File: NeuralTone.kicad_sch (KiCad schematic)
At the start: 95 parts, among them J1 USB-C PD, J2 Guitar, J3 Headphones, J4 USB-A Port, J5 Line Out, J6 5V Fan, J7 TF-01A, Q1 AON7421, Q2 IRLML6344, SW1 SW_Push, U1 AP2210N-3.3, U2 AP2210N-5.0, U3 CH224K, U4 MCP6022, U5 AMS1084CM-5.0, U6 AP2210N-3.3, U7 AP2171, U8 NAU8814YG, U9 DRTR5V0U2SR, Y1 OT322512MJBA4SL

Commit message: fix all footprints and 3d models
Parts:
- D1, D8: footprint Diode_SMD:D_SOD-123 -> NeuralTone:D_SOD-123
- D10, D6: footprint Package_TO_SOT_SMD:SOT-23-6_Handsoldering -> Package_TO_SOT_SMD:SOT-23-6
- D2, D4, D5: footprint Diode_SMD:D_SOD-123F -> NeuralTone:D_SOD-123F
- J1: footprint Connector_USB:USB_C_Receptacle_G-Switch_GT-USB-7010ASV -> NeuralTone:USB_C_Receptacle_G-Switch_GT-USB-7010ASV
- J2, J3, J5: footprint Connector_Audio:Jack_6.35mm_Neutrik_NMJ6HCD2_Horizontal -> NeuralTone:Jack_6.35mm_Neutrik_NMJ6HCD2_Horizontal
- J4: footprint Connector_USB:USB_A_CONNFLY_DS1095-WNR0 -> NeuralTone:USB_A_CONNFLY_DS1095-WNR0
- L1: footprint NeuralTone:104CDMCC_DS -> NeuralTone:L_Sunlord_MWSA0412S
- Q2: footprint Package_TO_SOT_SMD:SOT-23-3 -> Package_TO_SOT_SMD:SOT-23
- U7: footprint Package_TO_SOT_SMD:SOT-23-5_HandSoldering -> Package_TO_SOT_SMD:SOT-23-5
- U9: footprint Package_TO_SOT_SMD:SOT-143_Handsoldering -> NeuralTone:SOT-143
- Y1: footprint Crystal:Crystal_SMD_3225-4Pin_3.2x2.5mm -> NeuralTone:Crystal_SMD_3225-4Pin_3.2x2.5mm
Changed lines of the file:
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@@
       (effects (font (size 1.27 1.27)))
     )
-    (property "Footprint" "Package_TO_SOT_SMD:SOT-143_Handsoldering" (at 355.6 168.275 0)
+    (property "Footprint" "NeuralTone:SOT-143" (at 355.6 168.275 0)
       (effects (font (size 1.27 1.27)) hide)
     )
@@
       (effects (font (size 1.27 1.27)) (justify right))
     )
-    (property "Footprint" "Diode_SMD:D_SOD-123F" (at 271.145 167.259 0)
+    (property "Footprint" "NeuralTone:D_SOD-123F" (at 271.145 167.259 0)
       (effects (font (size 1.27 1.27)) hide)
     )
@@
       (effects (font (size 1.27 1.27)) (justify right))
     )
-    (property "Footprint" "Diode_SMD:D_SOD-123F" (at 271.145 140.589 0)
+    (property "Footprint" "NeuralTone:D_SOD-123F" (at 271.145 140.589 0)
       (effects (font (size 1.27 1.27)) hide)
     )
@@
       (effects (font (size 1.27 1.27)) (justify right))
     )
-    (property "Footprint" "Connector_USB:USB_A_CONNFLY_DS1095-WNR0" (at 372.745 148.59 0)
+    (property "Footprint" "NeuralTone:USB_A_CONNFLY_DS1095-WNR0" (at 372.745 148.59 0)
       (effects (font (size 1.27 1.27)) hide)
     )
@@
       (effects (font (size 1.27 1.27)))
     )
-    (property "Footprint" "Crystal:Crystal_SMD_3225-4Pin_3.2x2.5mm" (at 66.04 172.72 0)
+    (property "Footprint" "NeuralTone:Crystal_SMD_3225-4Pin_3.2x2.5mm" (at 66.04 172.72 0)
       (effects (font (size 1.27 1.27)) hide)
     )
@@
       (effects (font (size 1.27 1.27)) (justify left))
     )
-    (property "Footprint" "Package_TO_SOT_SMD:SOT-23-6_Handsoldering" (at 69.723 212.725 90)
+    (property "Footprint" "Package_TO_SOT_SMD:SOT-23-6" (at 69.723 212.725 90)
       (effects (font (size 1.27 1.27)) hide)
     )
@@
       (effects (font (size 1.27 1.27)) (justify left))
     )
-    (property "Footprint" "Diode_SMD:D_SOD-123" (at 238.76 224.79 90)
+    (property "Footprint" "NeuralTone:D_SOD-123" (at 238.76 224.79 90)
       (effects (font (size 1.27 1.27)) hide)
     )
@@
       (effects (font (size 1.27 1.27)) (justify left))
     )
-    (property "Footprint" "Diode_SMD:D_SOD-123F" (at 47.625 86.995 90)
+    (property "Footprint" "NeuralTone:D_SOD-123F" (at 47.625 86.995 90)
       (effects (font (size 1.27 1.27)) hide)
     )
@@
       (effects (font (size 1.27 1.27)) (justify left))
     )
-    (property "Footprint" "Package_TO_SOT_SMD:SOT-23-3" (at 235.585 234.315 0)
+    (property "Footprint" "Package_TO_SOT_SMD:SOT-23" (at 235.585 234.315 0)
       (effects (font (size 1.27 1.27)) hide)
     )
@@
       (effects (font (size 1.27 1.27)) (justify right))
     )
-    (property "Footprint" "Package_TO_SOT_SMD:SOT-23-6_Handsoldering" (at 69.215 245.11 90)
+    (property "Footprint" "Package_TO_SOT_SMD:SOT-23-6" (at 69.215 245.11 90)
       (effects (font (size 1.27 1.27)) hide)
     )
@@
       (effects (font (size 1.27 1.27)))
     )
-    (property "Footprint" "Connector_Audio:Jack_6.35mm_Neutrik_NMJ6HCD2_Horizontal" (at 279.4 141.605 0)
+    (property "Footprint" "NeuralTone:Jack_6.35mm_Neutrik_NMJ6HCD2_Horizontal" (at 279.4 141.605 0)
       (effects (font (size 1.27 1.27)) hide)
     )
@@
       (effects (font (size 1.27 1.27)))
     )
-    (property "Footprint" "Connector_USB:USB_C_Receptacle_G-Switch_GT-USB-7010ASV" (at 57.15 50.8 0)
+    (property "Footprint" "NeuralTone:USB_C_Receptacle_G-Switch_GT-USB-7010ASV" (at 57.15 50.8 0)
       (effects (font (size 1.27 1.27)) hide)
     )
@@
       (effects (font (size 1.27 1.27)) (justify right))
     )
-    (property "Footprint" "Connector_Audio:Jack_6.35mm_Neutrik_NMJ6HCD2_Horizontal" (at 266.065 58.42 0)
+    (property "Footprint" "NeuralTone:Jack_6.35mm_Neutrik_NMJ6HCD2_Horizontal" (at 266.065 58.42 0)
       (effects (font (size 1.27 1.27)) hide)
     )
@@
       (effects (font (size 1.27 1.27)))
     )
-    (property "Footprint" "Connector_Audio:Jack_6.35mm_Neutrik_NMJ6HCD2_Horizontal" (at 279.4 168.275 0)
+    (property "Footprint" "NeuralTone:Jack_6.35mm_Neutrik_NMJ6HCD2_Horizontal" (at 279.4 168.275 0)
       (effects (font (size 1.27 1.27)) hide)
     )
@@
       (effects (font (size 1.27 1.27)) (justify left))
     )
-    (property "Footprint" "Diode_SMD:D_SOD-123" (at 284.48 49.53 90)
+    (property "Footprint" "NeuralTone:D_SOD-123" (at 284.48 49.53 90)
       (effects (font (size 1.27 1.27)) hide)
     )
@@
       (effects (font (size 1.27 1.27)))
     )
-    (property "Footprint" "NeuralTone:104CDMCC_DS" (at 93.98 82.55 0)
+    (property "Footprint" "NeuralTone:L_Sunlord_MWSA0412S" (at 93.98 82.55 0)
       (effects (font (size 1.27 1.27)) hide)
     )
@@
       (effects (font (size 1.27 1.27)))
     )
-    (property "Footprint" "Package_TO_SOT_SMD:SOT-23-5_HandSoldering" (at 340.36 154.94 0)
+    (property "Footprint" "Package_TO_SOT_SMD:SOT-23-5" (at 340.36 154.94 0)
       (effects (font (size 1.27 1.27)) hide)
     )

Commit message: increase output cap for regulators
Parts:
- C15, C3, C5: value 1u -> 4.7u; LCSC C77083 -> C437557
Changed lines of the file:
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@@
     )
   )
+  (symbol (lib_id "Device:C_Small") (at 213.36 88.9 0) (unit 1)
+    (in_bom yes) (on_board yes) (dnp no) (fields_autoplaced)
+    (property "Reference" "C15" (at 215.9 87.6363 0)
+      (effects (font (size 1.27 1.27)) (justify left))
+    )
+    (property "Value" "4.7u" (at 215.9 90.1763 0)
+      (effects (font (size 1.27 1.27)) (justify left))
+    )
+    (property "Footprint" "Capacitor_SMD:C_0805_2012Metric_Pad1.18x1.45mm_HandSolder" (at 213.36 88.9 0)
+      (effects (font (size 1.27 1.27)) hide)
+    )
+    (property "Datasheet" "~" (at 213.36 88.9 0)
+      (effects (font (size 1.27 1.27)) hide)
+    )
+    (property "LCSC" "C437557" (at 213.36 88.9 0)
+      (effects (font (size 1.27 1.27)) hide)
+    )
+    (pin "1")
+    (pin "2")
+    (instances
+      (project "NeuralTone"
+        (path "/ac6c2b5b-00d5-42f9-9826-f03f3806195c"
+          (reference "C15") (unit 1)
+        )
+      )
+    )
+  )
   (symbol (lib_id "Device:R_Small") (at 52.07 95.25 0) (unit 1)
     (in_bom yes) (on_board yes) (dnp no) (fields_autoplaced)
@@
     )
   )
-  (symbol (lib_id "Device:C_Small") (at 213.36 53.975 0) (unit 1)
-    (in_bom yes) (on_board yes) (dnp no)
-    (property "Reference" "C5" (at 215.9 52.705 0)
-      (effects (font (size 1.27 1.27)) (justify left))
-    )
-    (property "Value" "1u" (at 215.9 55.245 0)
-      (effects (font (size 1.27 1.27)) (justify left))
-    )
-    (property "Footprint" "Capacitor_SMD:C_0805_2012Metric_Pad1.18x1.45mm_HandSolder" (at 213.36 53.975 0)
-      (effects (font (size 1.27 1.27)) hide)
-    )
-    (property "Datasheet" "~" (at 213.36 53.975 0)
-      (effects (font (size 1.27 1.27)) hide)
-    )
-    (property "LCSC" "C77083" (at 213.36 53.975 0)
-      (effects (font (size 1.27 1.27)) hide)
-    )
-    (pin "1")
-    (pin "2")
-    (instances
-      (project "NeuralTone"
-        (path "/ac6c2b5b-00d5-42f9-9826-f03f3806195c"
-          (reference "C5") (unit 1)
-        )
-      )
-    )
-  )
   (symbol (lib_id "Device:C_Small") (at 264.795 141.605 180) (unit 1)
     (in_bom yes) (on_board yes) (dnp no)
@@
     )
   )
+  (symbol (lib_id "Device:C_Small") (at 163.195 53.975 0) (unit 1)
+    (in_bom yes) (on_board yes) (dnp no) (fields_autoplaced)
+    (property "Reference" "C3" (at 165.735 52.7113 0)
+      (effects (font (size 1.27 1.27)) (justify left))
+    )
+    (property "Value" "4.7u" (at 165.735 55.2513 0)
+      (effects (font (size 1.27 1.27)) (justify left))
+    )
+    (property "Footprint" "Capacitor_SMD:C_0805_2012Metric_Pad1.18x1.45mm_HandSolder" (at 163.195 53.975 0)
+      (effects (font (size 1.27 1.27)) hide)
+    )
+    (property "Datasheet" "~" (at 163.195 53.975 0)
+      (effects (font (size 1.27 1.27)) hide)
+    )
+    (property "LCSC" "C437557" (at 163.195 53.975 0)
+      (effects (font (size 1.27 1.27)) hide)
+    )
+    (pin "1")
+    (pin "2")
+    (instances
+      (project "NeuralTone"
+        (path "/ac6c2b5b-00d5-42f9-9826-f03f3806195c"
+          (reference "C3") (unit 1)
+        )
+      )
+    )
+  )
   (symbol (lib_id "power:+9V") (at 189.23 47.625 0) (unit 1)
     (in_bom yes) (on_board yes) (dnp no) (fields_autoplaced)
@@
     )
   )
+  (symbol (lib_id "Device:C_Small") (at 213.36 53.975 0) (unit 1)
+    (in_bom yes) (on_board yes) (dnp no) (fields_autoplaced)
+    (property "Reference" "C5" (at 215.9 52.7113 0)
+      (effects (font (size 1.27 1.27)) (justify left))
+    )
+    (property "Value" "4.7u" (at 215.9 55.2513 0)
+      (effects (font (size 1.27 1.27)) (justify left))
+    )
+    (property "Footprint" "Capacitor_SMD:C_0805_2012Metric_Pad1.18x1.45mm_HandSolder" (at 213.36 53.975 0)
+      (effects (font (size 1.27 1.27)) hide)
+    )
+    (property "Datasheet" "~" (at 213.36 53.975 0)
+      (effects (font (size 1.27 1.27)) hide)
+    )
+    (property "LCSC" "C437557" (at 213.36 53.975 0)
+      (effects (font (size 1.27 1.27)) hide)
+    )
+    (pin "1")
+    (pin "2")
+    (instances
+      (project "NeuralTone"
+        (path "/ac6c2b5b-00d5-42f9-9826-f03f3806195c"
+          (reference "C5") (unit 1)
+        )
+      )
+    )
+  )
   (symbol (lib_id "power:GND") (at 163.195 61.595 0) (unit 1)
     (in_bom yes) (on_board yes) (dnp no)
@@
     )
   )
-  (symbol (lib_id "Device:C_Small") (at 163.195 53.975 0) (unit 1)
-    (in_bom yes) (on_board yes) (dnp no)
-    (property "Reference" "C3" (at 165.735 52.705 0)
-      (effects (font (size 1.27 1.27)) (justify left))
-    )
-    (property "Value" "1u" (at 165.735 55.245 0)
-      (effects (font (size 1.27 1.27)) (justify left))
-    )
-    (property "Footprint" "Capacitor_SMD:C_0805_2012Metric_Pad1.18x1.45mm_HandSolder" (at 163.195 53.975 0)
-      (effects (font (size 1.27 1.27)) hide)
-    )
-    (property "Datasheet" "~" (at 163.195 53.975 0)
-      (effects (font (size 1.27 1.27)) hide)
-    )
-    (property "LCSC" "C77083" (at 163.195 53.975 0)
-      (effects (font (size 1.27 1.27)) hide)
-    )
-    (pin "1")
-    (pin "2")
-    (instances
-      (project "NeuralTone"
-        (path "/ac6c2b5b-00d5-42f9-9826-f03f3806195c"
-          (reference "C3") (unit 1)
-        )
-      )
-    )
-  )
   (symbol (lib_id "Device:LED_Small") (at 176.53 219.71 180) (unit 1)
     (in_bom yes) (on_board yes) (dnp no)
@@
         )
       )
-    )
-  )
-  (symbol (lib_id "Device:C_Small") (at 213.36 88.9 0) (unit 1)
-    (in_bom yes) (on_board yes) (dnp no)
-    (property "Reference" "C15" (at 215.9 87.63 0)
-      (effects (font (size 1.27 1.27)) (justify left))
-    )
-    (property "Value" "1u" (at 215.9 90.17 0)
-      (effects (font (size 1.27 1.27)) (justify left))
-    )
-    (property "Footprint" "Capacitor_SMD:C_0805_2012Metric_Pad1.18x1.45mm_HandSolder" (at 213.36 88.9 0)
-      (effects (font (size 1.27 1.27)) hide)
-    )
-    (property "Datasheet" "~" (at 213.36 88.9 0)
-      (effects (font (size 1.27 1.27)) hide)
-    )
-    (property "LCSC" "C77083" (at 213.36 88.9 0)
-      (effects (font (size 1.27 1.27)) hide)
-    )
-    (pin "1")
-    (pin "2")
-    (instances
-      (project "NeuralTone"
-        (path "/ac6c2b5b-00d5-42f9-9826-f03f3806195c"
-          (reference "C15") (unit 1)
-        )
-      )

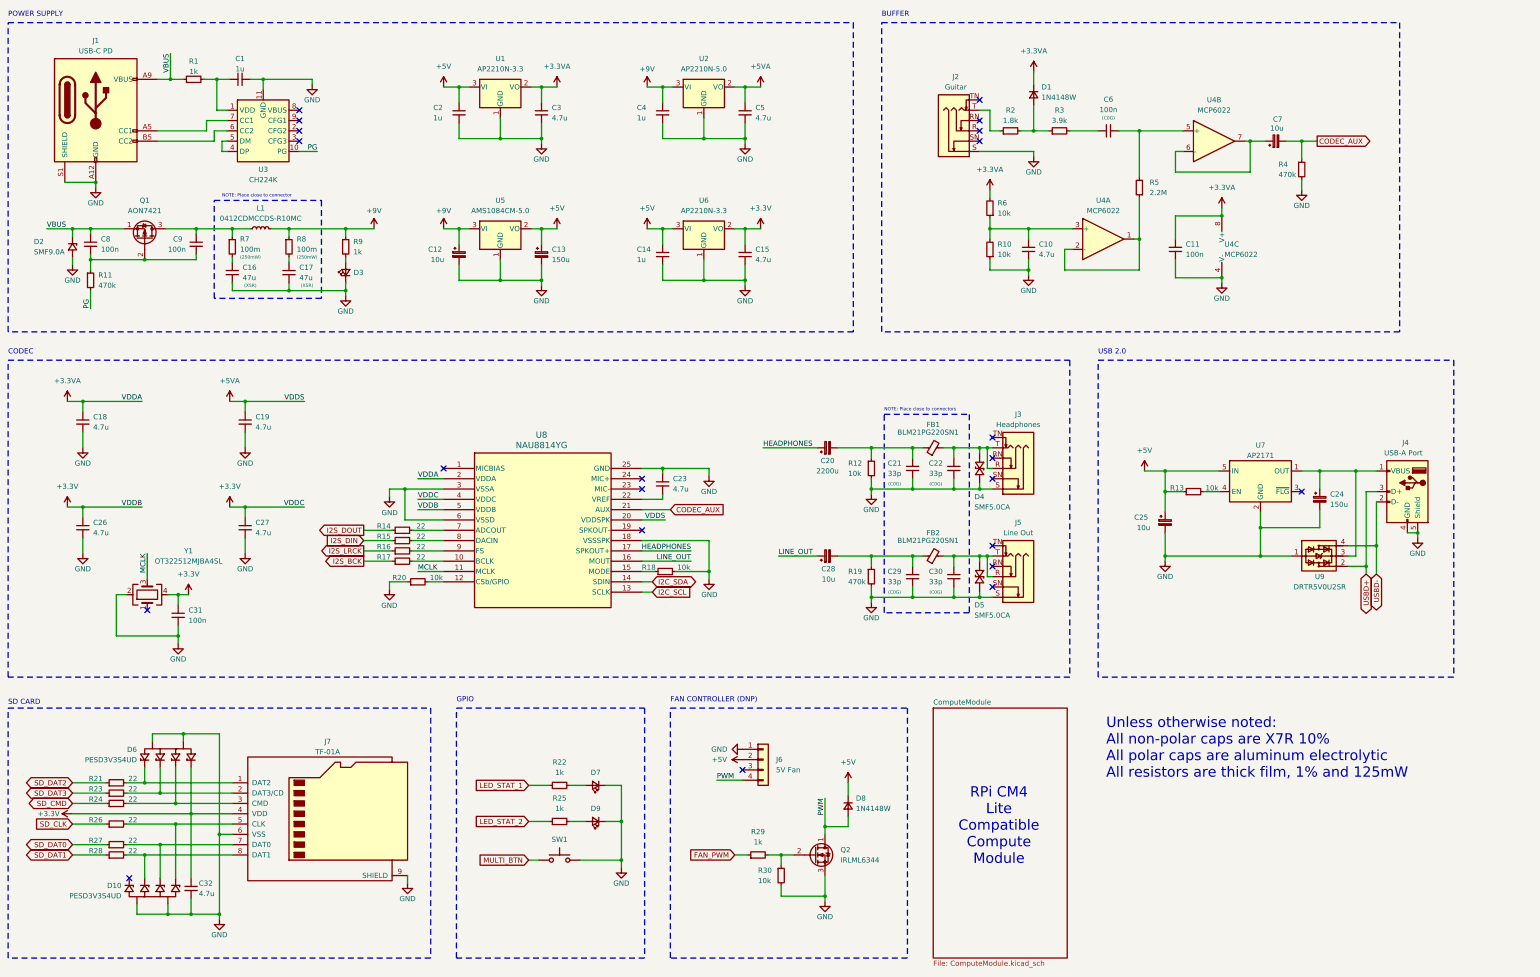
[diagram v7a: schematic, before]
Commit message: switch to 0603 footprints
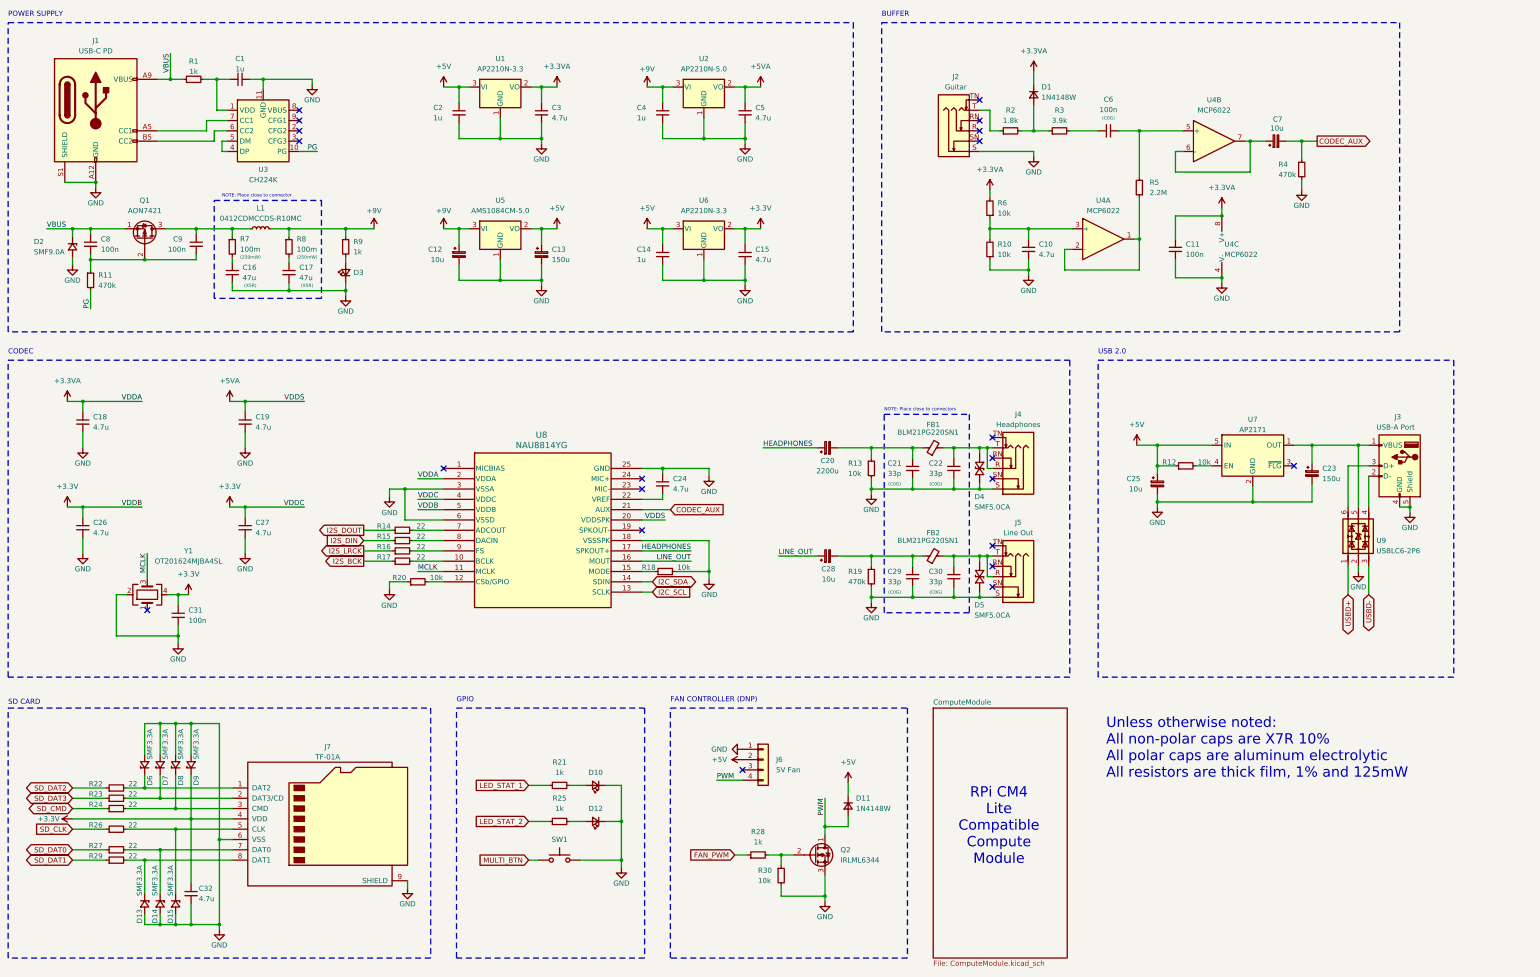
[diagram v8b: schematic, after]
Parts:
- removed D10, D6: PESD3V3S4UD, Package_TO_SOT_SMD:SOT-23-6, symbol NeuralTone:D_TVS_Quad
- removed U9: DRTR5V0U2SR, NeuralTone:SOT-143, symbol NeuralTone:DRTR5V0U2SR
- added D13, D14, D15, D6, D7, D8, D9: SMF3.3A, NeuralTone:D_SOD-123F, symbol NeuralTone:D_TVS_Single
- added U9: USBLC6-2P6, Package_TO_SOT_SMD:SOT-666, symbol NeuralTone:USBLC6-2P6
- C1, C10, C11, C14, C15, C18, C19, C2, C21, C22, C26, C27, C29, C3, C30, C31, C32, C4, C5, C8, C9: footprint Capacitor_SMD:C_0805_2012Metric_Pad1.18x1.45mm_HandSolder -> Capacitor_SMD:C_0603_1608Metric
- C16, C17: footprint Capacitor_SMD:C_1210_3225Metric_Pad1.33x2.70mm_HandSolder -> Capacitor_SMD:C_1210_3225Metric
- C24: renamed from C23; footprint Capacitor_SMD:C_0805_2012Metric_Pad1.18x1.45mm_HandSolder -> Capacitor_SMD:C_0603_1608Metric
- C6: footprint Capacitor_SMD:C_1206_3216Metric_Pad1.33x1.80mm_HandSolder -> Capacitor_SMD:C_1206_3216Metric
- D10: renamed from D7; footprint LED_SMD:LED_1206_3216Metric_Pad1.42x1.75mm_HandSolder -> LED_SMD:LED_1206_3216Metric
- D12: renamed from D9; footprint LED_SMD:LED_1206_3216Metric_Pad1.42x1.75mm_HandSolder -> LED_SMD:LED_1206_3216Metric
- D3: footprint LED_SMD:LED_1206_3216Metric_Pad1.42x1.75mm_HandSolder -> LED_SMD:LED_1206_3216Metric
- FB1, FB2: footprint Inductor_SMD:L_0805_2012Metric_Pad1.15x1.40mm_HandSolder -> Inductor_SMD:L_0805_2012Metric
- R1, R10, R11, R14, R15, R16, R17, R18, R19, R2, R20, R23, R24, R25, R26, R27, R3, R30, R4, R5, R6, R7, R8, R9: footprint Resistor_SMD:R_0805_2012Metric_Pad1.20x1.40mm_HandSolder -> Resistor_SMD:R_0603_1608Metric
- R12: renamed from R13; footprint Resistor_SMD:R_0805_2012Metric_Pad1.20x1.40mm_HandSolder -> Resistor_SMD:R_0603_1608Metric
- R13: renamed from R12; footprint Resistor_SMD:R_0805_2012Metric_Pad1.20x1.40mm_HandSolder -> Resistor_SMD:R_0603_1608Metric
- R21: renamed from R22; footprint Resistor_SMD:R_0805_2012Metric_Pad1.20x1.40mm_HandSolder -> Resistor_SMD:R_0603_1608Metric
- R22: renamed from R21; footprint Resistor_SMD:R_0805_2012Metric_Pad1.20x1.40mm_HandSolder -> Resistor_SMD:R_0603_1608Metric
- R28: renamed from R29; footprint Resistor_SMD:R_0805_2012Metric_Pad1.20x1.40mm_HandSolder -> Resistor_SMD:R_0603_1608Metric
- R29: renamed from R28; footprint Resistor_SMD:R_0805_2012Metric_Pad1.20x1.40mm_HandSolder -> Resistor_SMD:R_0603_1608Metric
- U5: footprint Package_TO_SOT_SMD:TO-263-3_TabPin2 -> Package_TO_SOT_SMD:SOT-23
- U8: footprint NeuralTone:QFN-24_4X4_NUV-M -> Package_DFN_QFN:QFN-24-1EP_4x4mm_P0.5mm_EP2.6x2.6mm_ThermalVias
- Y1: value OT322512MJBA4SL -> OT201624MJBA4SL; footprint NeuralTone:Crystal_SMD_3225-4Pin_3.2x2.5mm -> Crystal:Crystal_SMD_2016-4Pin_2.0x1.6mm; LCSC C725989 -> C725986
- renumbered C24 to C23, D8 to D11, J4 to J3, J3 to J4
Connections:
- net +3.3V: now also D9.1 (K)
- net GND: now also D13.2 (A), D14.2 (A), D15.2 (A), D6.2 (A), D7.2 (A), D8.2 (A), D9.2 (A), U9.2
- net USBD+: now also U9.1; no longer J3.3 (D+)
- net USBD-: now also U9.3; no longer J3.2 (D-)
- net at C23.1, J3.1 (VBUS), U7.1 (OUT): now also U9.5
- net at J7.3 (CMD), R24.2: now also D8.1 (K)
- net at J7.1 (DAT2), R22.2: now also D6.1 (K)
- net at J7.2 (DAT3/CD), R23.2: now also D7.1 (K)
- net at J7.5 (CLK), R26.2: now also D15.1 (K)
- net at J7.7 (DAT0), R27.2: now also D14.1 (K)
- net at J7.8 (DAT1), R29.2: now also D13.1 (K)
- new net: J3.2 (D-), U9.4
- new net: J3.3 (D+), U9.6
- no-connect marks 22 -> 21
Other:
- moved on the sheet: C23, C25, C32, J3, J7, R12, R22, R23, R24, R26, R27, R29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
